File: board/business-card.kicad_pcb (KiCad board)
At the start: 2 copper layers, 88.9 x 50.8 mm, 36 parts, among them J1 Conn_01x06, SW1 SW_SPDT, SW2 Mutual_Capacitance_Button, SW3 Mutual_Capacitance_Button, SW4 Mutual_Capacitance_Button, SW5 Mutual_Capacitance_Button, SW6 Mutual_Capacitance_Button, SW7 Mutual_Capacitance_Button, U1 ATtiny1616-S

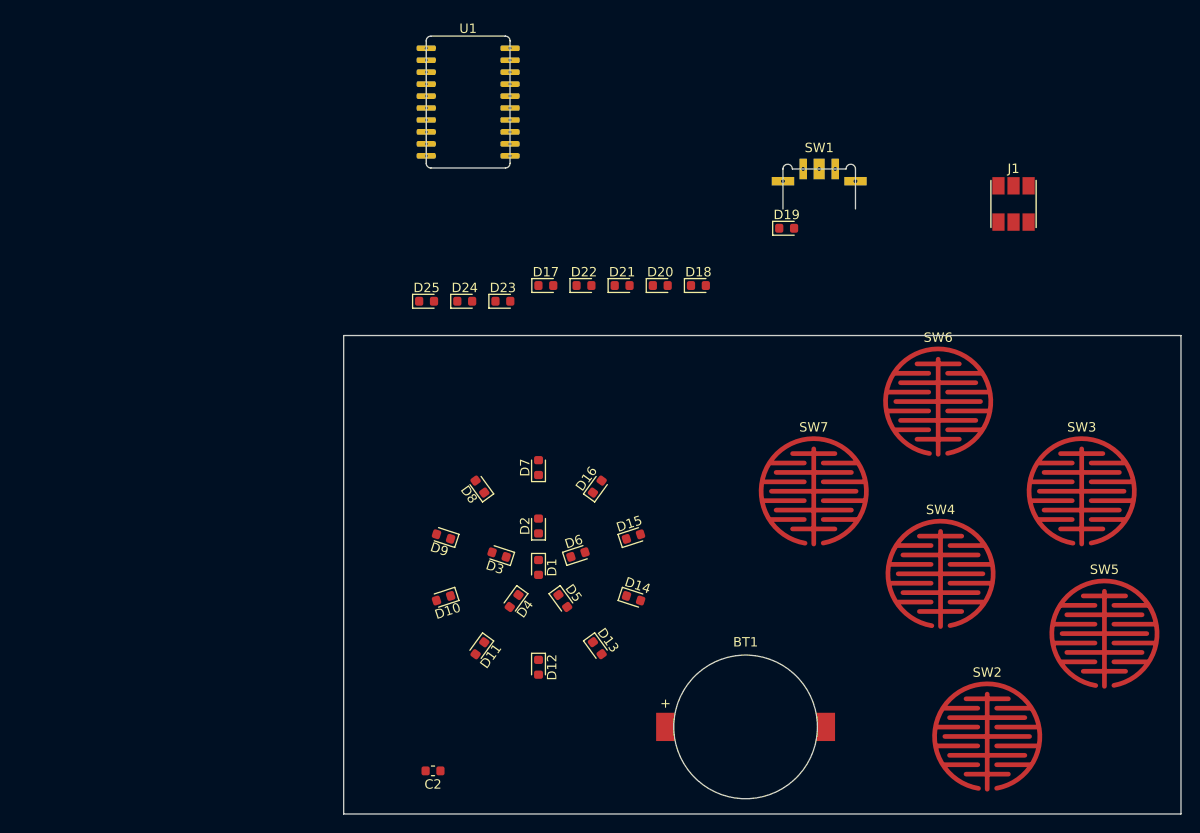
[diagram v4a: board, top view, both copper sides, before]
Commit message: Added through board footprint for XZCBD led.
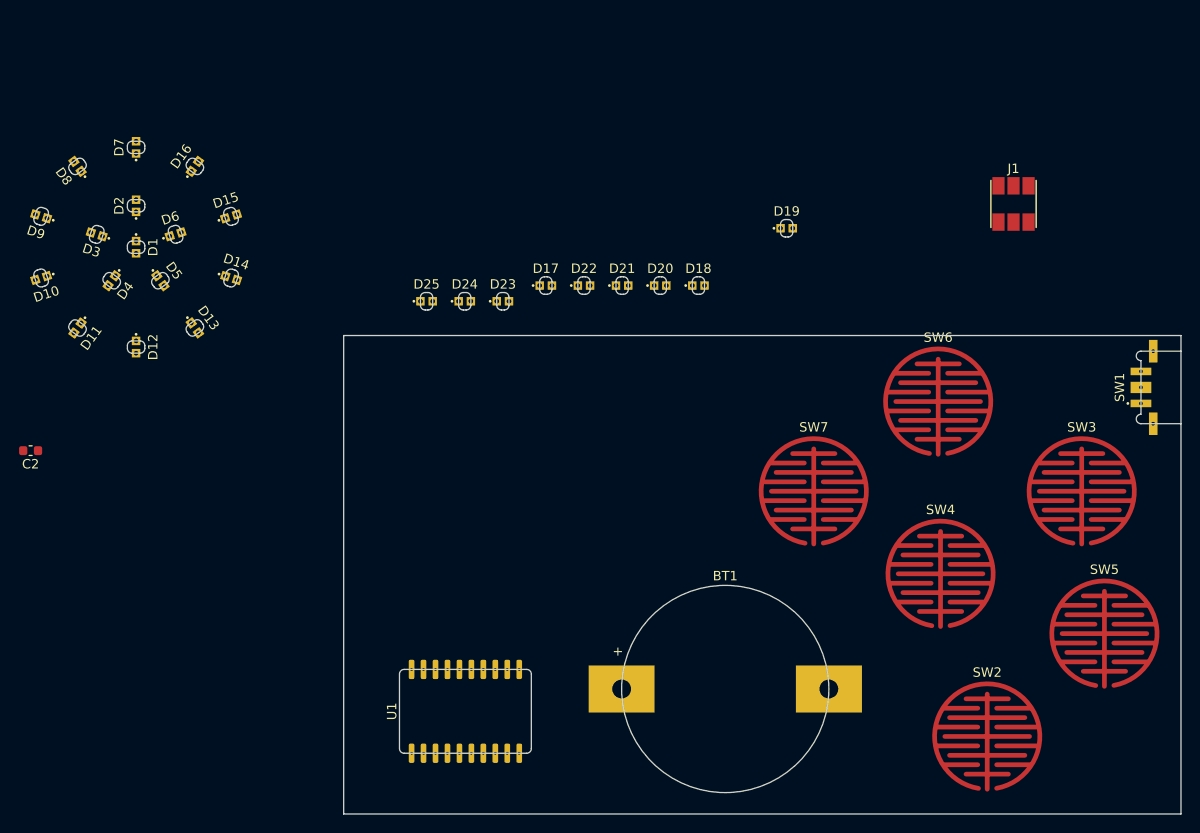
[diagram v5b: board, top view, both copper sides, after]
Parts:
- BT1: footprint renata:CR1216_MFR_SM -> business-card:CR2016_MFR_SM_through_board_mount
- D1, D10, D11, D12, D13, D14, D15, D16, D17, D18, D19, D2, D20, D21, D22, D23, D24, D25, D3, D4, D5, D6, D7, D8, D9: footprint LED_SMD:LED_0603_1608Metric -> business-card:XZCBD53W-6_through_board_mount
- SW1: footprint colinholzman:JSX08001SAQNL_through_board_mount -> business-card:JSX08001SAQNL_through_board_mount
- U1: footprint colinholzman:SOIC-20W_7.5x12.8mm_P1.27mm_through_board_mount -> business-card:SOIC-20W_7.5x12.8mm_P1.27mm_through_board_mount
- moved U1 64.7 mm to (12.9, 39.9), turned to 90 degrees
- moved D1 54.6 mm to (-22.0, -9.38)
- moved D10 54.6 mm to (-32.1, -6.11)
- moved D11 54.6 mm to (-28.3, -0.80)
- moved D12 54.6 mm to (-22.0, 1.22)
- moved D14 54.6 mm to (-11.9, -6.11)
- moved D2 54.6 mm to (-22.0, -13.8)
- moved D3 54.6 mm to (-26.2, -10.7)
- moved D4 54.6 mm to (-24.6, -5.82)
- moved D6 54.6 mm to (-17.8, -10.7)
- moved D7 54.6 mm to (-22.0, -20.0)
- moved D8 54.6 mm to (-28.3, -18.0)
- moved D9 54.6 mm to (-32.1, -12.7)
- moved C2 54.6 mm to (-33.2, 12.2)
- moved D13 54.6 mm to (-15.8, -0.81)
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
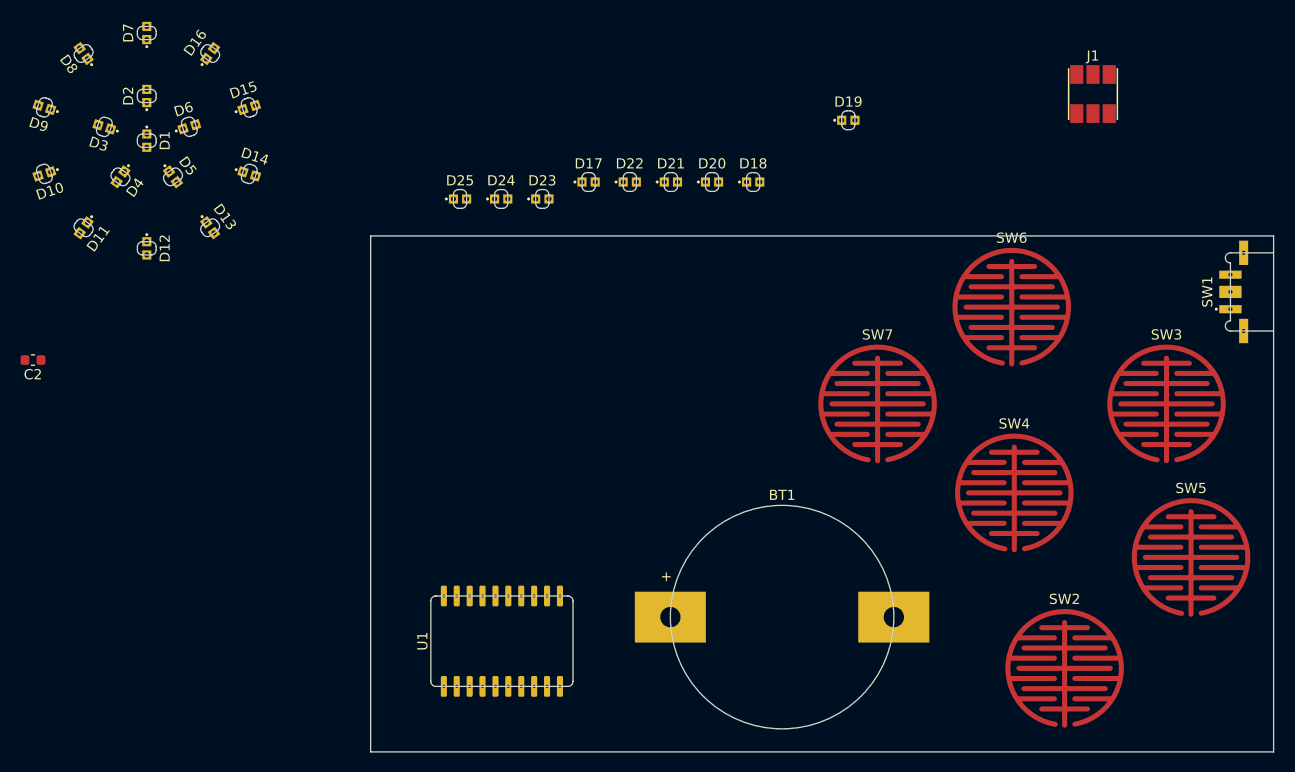
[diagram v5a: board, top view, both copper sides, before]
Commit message: Added 0603 through board mount, arranged leds in grid.
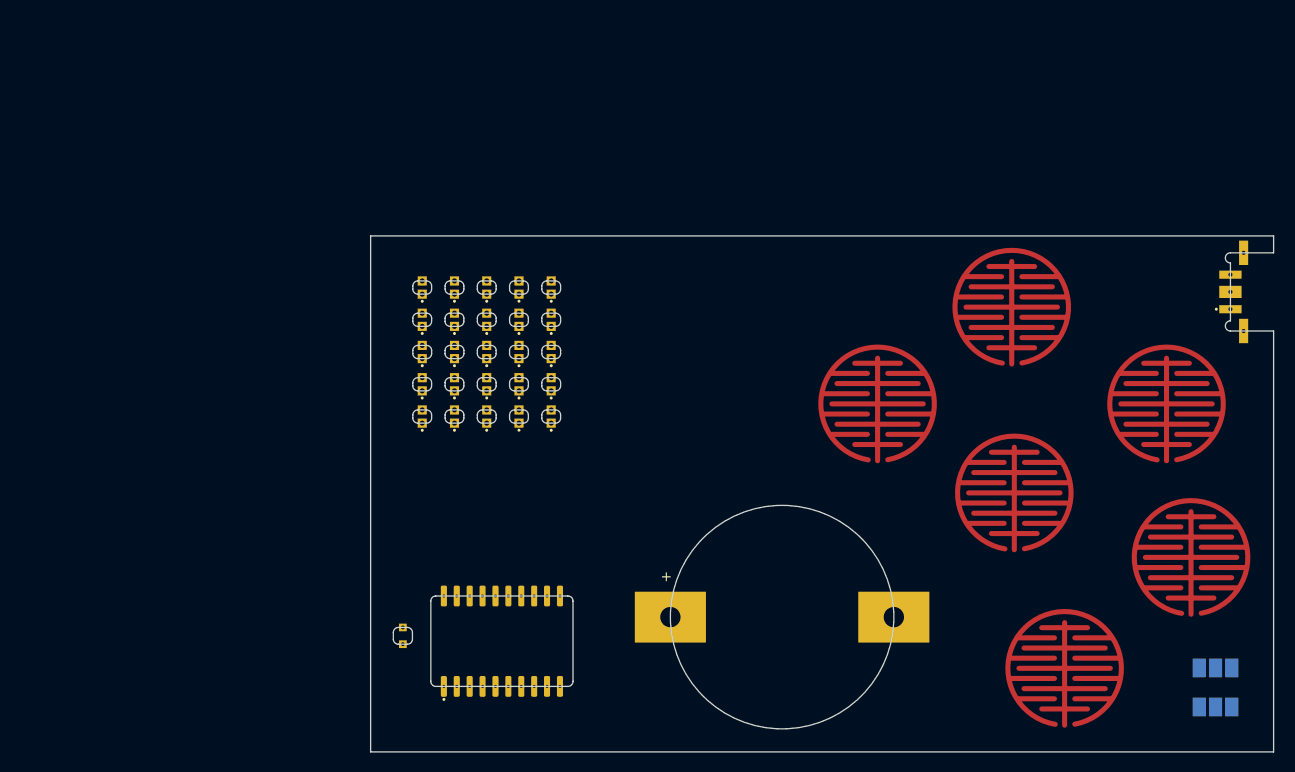
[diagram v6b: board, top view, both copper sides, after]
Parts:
- C2: footprint Capacitor_SMD:C_0603_1608Metric -> business-card:0603_through_board_mount
- J1: moved to B.Cu
- moved J1 59.7 mm to (83.2, 44.5), turned to 180 degrees
- moved D8 50.2 mm to (14.6, 8.26), turned to 90 degrees
- moved D19 46.0 mm to (11.4, 17.8), turned to 90 degrees
- moved C2 45.4 mm to (3.17, 39.4), turned to 270 degrees
- moved D16 44.6 mm to (14.6, 14.6), turned to 90 degrees
- moved D7 44.4 mm to (14.6, 5.08)
- moved D9 44.3 mm to (5.08, 11.4), turned to 90 degrees
- moved D10 42.6 mm to (5.08, 14.6), turned to 90 degrees
- moved D11 38.5 mm to (8.26, 11.4), turned to 90 degrees
- moved D3 37.9 mm to (8.26, 5.08), turned to 90 degrees
- moved D18 37.4 mm to (8.26, 17.8), turned to 90 degrees
- moved D15 35.9 mm to (14.6, 11.4), turned to 90 degrees
- moved D4 35.8 mm to (8.26, 8.26), turned to 90 degrees
- moved D2 34.9 mm to (5.08, 8.26)
- moved D6 34.9 mm to (11.4, 8.26), turned to 90 degrees
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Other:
- outline, holes or cut-outs redrawn
- rule pad_to_mask_clearance: 0.051 -> 0

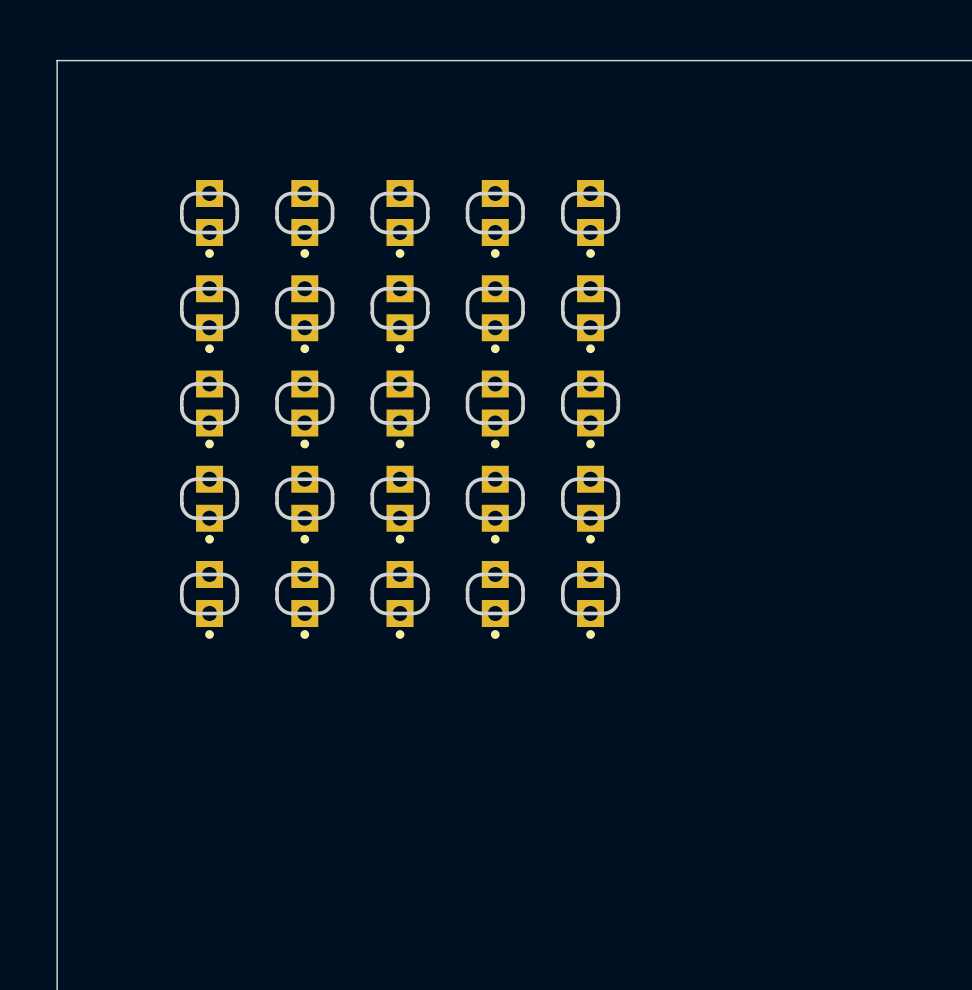
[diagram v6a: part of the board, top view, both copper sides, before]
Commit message: Added another row and column of leds.
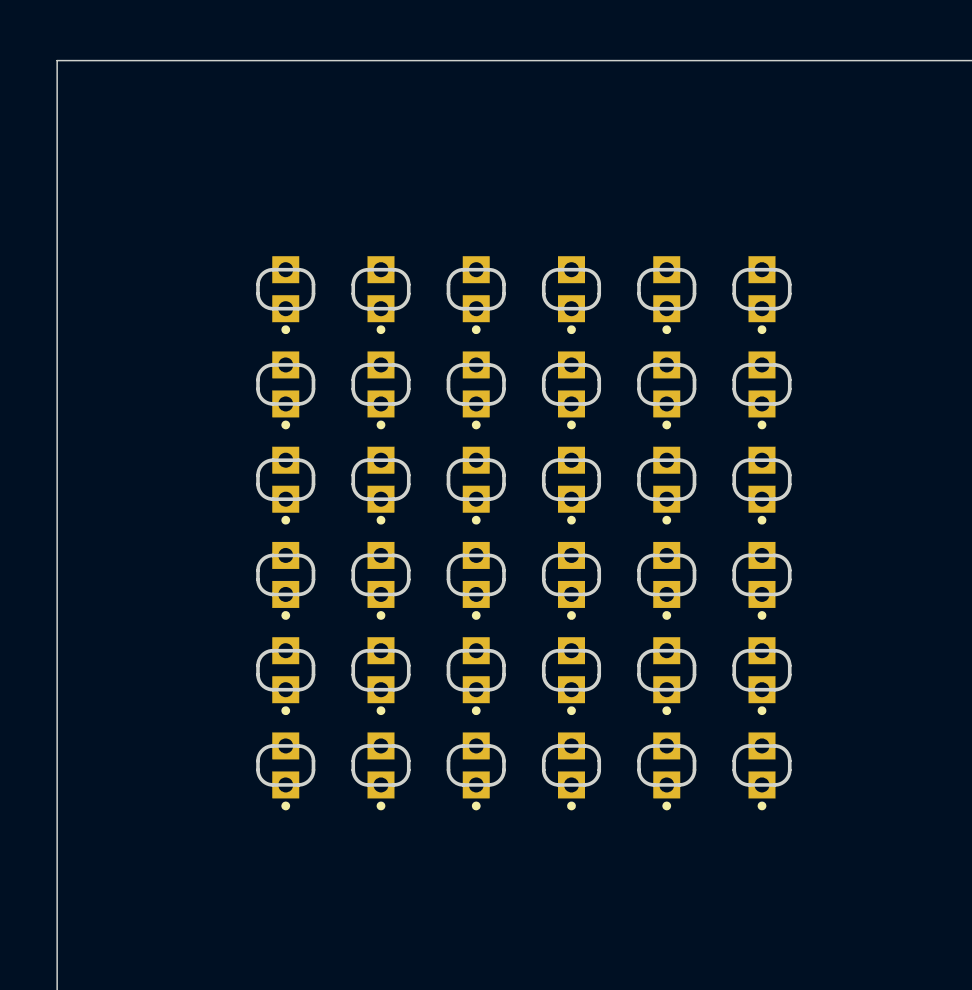
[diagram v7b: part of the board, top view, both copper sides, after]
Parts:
- added D26: LED, business-card:XZCBD53W-6_through_board_mount, F.Cu at (7.62, 23.5)
- added D27: LED, business-card:XZCBD53W-6_through_board_mount, F.Cu at (10.8, 23.5)
- added D28: LED, business-card:XZCBD53W-6_through_board_mount, F.Cu at (14.0, 23.5)
- added D29: LED, business-card:XZCBD53W-6_through_board_mount, F.Cu at (17.1, 23.5)
- added D30: LED, business-card:XZCBD53W-6_through_board_mount, F.Cu at (20.3, 23.5)
- added D31: LED, business-card:XZCBD53W-6_through_board_mount, F.Cu at (23.5, 7.62)
- added D32: LED, business-card:XZCBD53W-6_through_board_mount, F.Cu at (23.5, 10.8)
- added D33: LED, business-card:XZCBD53W-6_through_board_mount, F.Cu at (23.5, 14.0)
- added D34: LED, business-card:XZCBD53W-6_through_board_mount, F.Cu at (23.5, 17.1)
- added D35: LED, business-card:XZCBD53W-6_through_board_mount, F.Cu at (23.5, 20.3)
- added D36: LED, business-card:XZCBD53W-6_through_board_mount, F.Cu at (23.5, 23.5)
- moved D13 3.59 mm to (14.0, 14.0)
- moved D5 3.59 mm to (14.0, 7.62)
- moved D9 3.59 mm to (7.62, 14.0)
- moved D1 3.59 mm to (7.62, 7.62)
- moved D10 3.59 mm to (7.62, 17.1)
- moved D11 3.59 mm to (10.8, 14.0)
- moved D14 3.59 mm to (14.0, 17.1)
- moved D15 3.59 mm to (17.1, 14.0)
- moved D17 3.59 mm to (7.62, 20.3)
- moved D19 3.59 mm to (14.0, 20.3)
- moved D2 3.59 mm to (7.62, 10.8)
- moved D21 3.59 mm to (20.3, 7.62)
- moved D23 3.59 mm to (20.3, 14.0)
- moved D3 3.59 mm to (10.8, 7.62)
- moved D6 3.59 mm to (14.0, 10.8)
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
